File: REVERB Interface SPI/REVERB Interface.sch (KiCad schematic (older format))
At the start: 50 parts, among them J1 RPiZeroW, J2 Iridium, J3 APRS, J4 Antenna, M1 MountingHole_Pad, M2 MountingHole_Pad, M3 MountingHole_Pad, M4 MountingHole_Pad, M5 PiMount, M6 PiMount, M7 PiMount, M8 PiMount, U1 LSM9DS1BOB, U2 MAX3232, U3 SC16IS752IPW, Y1 1.8432MHz

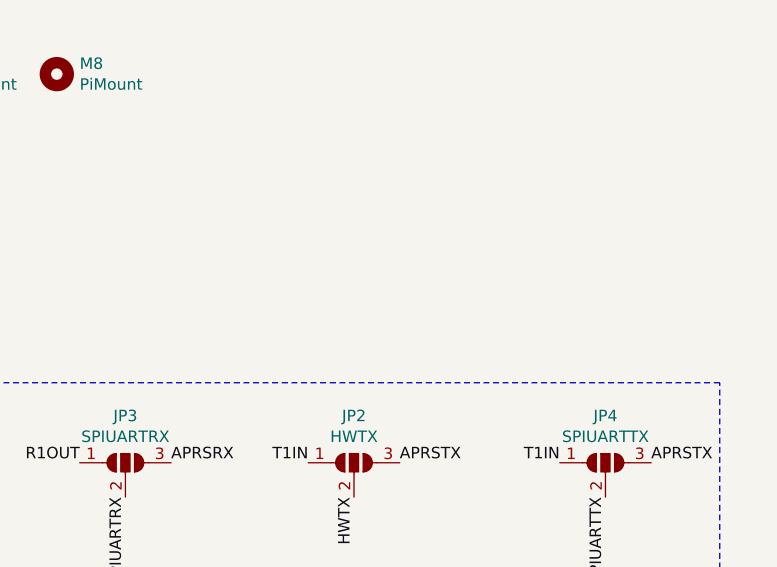
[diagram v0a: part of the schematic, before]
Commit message: Add LEDs for all used PDMs
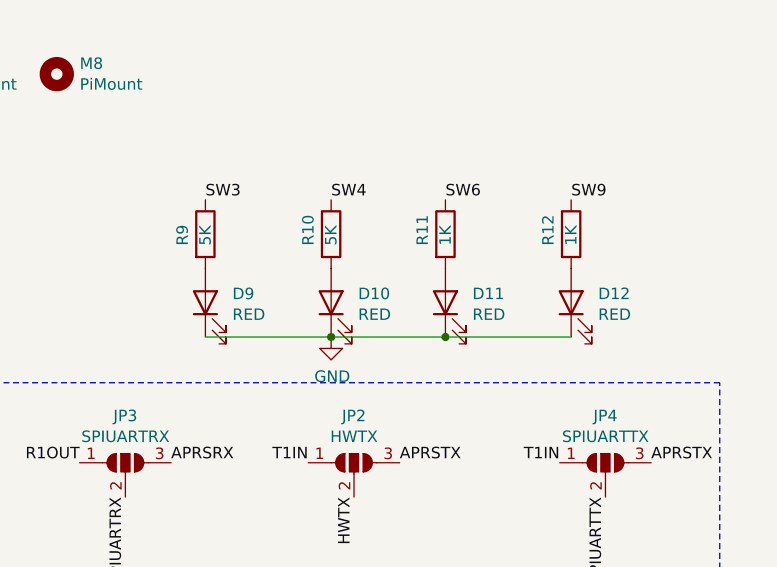
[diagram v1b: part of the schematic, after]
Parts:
- added D10, D11, D12, D9: RED, LED_SMD:LED_0805_2012Metric_Pad1.15x1.40mm_HandSolder, symbol Device:LED
- added R10, R9: 5K, Resistor_SMD:R_0805_2012Metric_Pad1.20x1.40mm_HandSolder, symbol Device:R
- added R11, R12: 1K, Resistor_SMD:R_0805_2012Metric_Pad1.20x1.40mm_HandSolder, symbol Device:R
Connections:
- net GND: now also D10.1 (K), D11.1 (K), D12.1 (K), D9.1 (K)
- net SW3: now also R9.1
- net SW4: now also R10.1
- net SW6: now also R11.1
- net SW9: now also R12.1
- new net: D9.2 (A), R9.2
- new net: D10.2 (A), R10.2
- new net: D11.2 (A), R11.2
- new net: D12.2 (A), R12.2
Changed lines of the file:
@@
 Text Label 6100 2150 0    50   ~ 0
 RTS
+$Comp
+L Device:LED D9
+U 1 1 6164D690
+P 9150 3200
+F 0 "D9" V 9189 3082 50  0000 R CNN
+F 1 "RED" V 9098 3082 50  0000 R CNN
+F 2 "LED_SMD:LED_0805_2012Metric_Pad1.15x1.40mm_HandSolder" H 9150 3200 50  0001 C CNN
+F 3 "~" H 9150 3200 50  0001 C CNN
+	1    9150 3200
+	0    -1   -1   0
+$EndComp
+$Comp
+L Device:R R9
+U 1 1 6164D696
+P 9150 2900
+F 0 "R9" V 9050 2850 50  0000 L CNN
+F 1 "5K" V 9150 2850 50  0000 L CNN
+F 2 "Resistor_SMD:R_0805_2012Metric_Pad1.20x1.40mm_HandSolder" V 9080 2900 50  0001 C CNN
+F 3 "~" H 9150 2900 50  0001 C CNN
+	1    9150 2900
+	1    0    0    -1
+$EndComp
+$Comp
+L Device:LED D10
+U 1 1 61656747
+P 9700 3200
+F 0 "D10" V 9739 3082 50  0000 R CNN
+F 1 "RED" V 9648 3082 50  0000 R CNN
+F 2 "LED_SMD:LED_0805_2012Metric_Pad1.15x1.40mm_HandSolder" H 9700 3200 50  0001 C CNN
+F 3 "~" H 9700 3200 50  0001 C CNN
+	1    9700 3200
+	0    -1   -1   0
+$EndComp
+$Comp
+L Device:R R10
+U 1 1 6165674D
+P 9700 2900
+F 0 "R10" V 9600 2850 50  0000 L CNN
+F 1 "5K" V 9700 2850 50  0000 L CNN
+F 2 "Resistor_SMD:R_0805_2012Metric_Pad1.20x1.40mm_HandSolder" V 9630 2900 50  0001 C CNN
+F 3 "~" H 9700 2900 50  0001 C CNN
+	1    9700 2900
+	1    0    0    -1
+$EndComp
+$Comp
+L Device:LED D11
+U 1 1 6165A88F
+P 10200 3200
+F 0 "D11" V 10239 3082 50  0000 R CNN
+F 1 "RED" V 10148 3082 50  0000 R CNN
+F 2 "LED_SMD:LED_0805_2012Metric_Pad1.15x1.40mm_HandSolder" H 10200 3200 50  0001 C CNN
+F 3 "~" H 10200 3200 50  0001 C CNN
+	1    10200 3200
+	0    -1   -1   0
+$EndComp
+$Comp
+L Device:R R11
+U 1 1 6165A895
+P 10200 2900
+F 0 "R11" V 10100 2850 50  0000 L CNN
+F 1 "1K" V 10200 2850 50  0000 L CNN
+F 2 "Resistor_SMD:R_0805_2012Metric_Pad1.20x1.40mm_HandSolder" V 10130 2900 50  0001 C CNN
+F 3 "~" H 10200 2900 50  0001 C CNN
+	1    10200 2900
+	1    0    0    -1
+$EndComp
+Text Label 9150 2750 0    50   ~ 0
+SW3
+Text Label 9700 2750 0    50   ~ 0
+SW4
+Text Label 10200 2750 0    50   ~ 0
+SW6
+Wire Wire Line
+	9150 3350 9700 3350
+Connection ~ 9700 3350
+Wire Wire Line
+	9700 3350 10200 3350
+$Comp
+L power:GND #PWR?
+U 1 1 61664C9F
+P 9700 3350
+F 0 "#PWR?" H 9700 3100 50  0001 C CNN
+F 1 "GND" H 9705 3177 50  0000 C CNN
+F 2 "" H 9700 3350 50  0001 C CNN
+F 3 "" H 9700 3350 50  0001 C CNN
+	1    9700 3350
+	1    0    0    -1
+$EndComp
+$Comp
+L Device:LED D12
+U 1 1 61666765
+P 10750 3200
+F 0 "D12" V 10789 3082 50  0000 R CNN
+F 1 "RED" V 10698 3082 50  0000 R CNN
+F 2 "LED_SMD:LED_0805_2012Metric_Pad1.15x1.40mm_HandSolder" H 10750 3200 50  0001 C CNN
+F 3 "~" H 10750 3200 50  0001 C CNN
+	1    10750 3200
+	0    -1   -1   0
+$EndComp
+$Comp
+L Device:R R12
+U 1 1 6166676B
+P 10750 2900
+F 0 "R12" V 10650 2850 50  0000 L CNN
+F 1 "1K" V 10750 2850 50  0000 L CNN
+F 2 "Resistor_SMD:R_0805_2012Metric_Pad1.20x1.40mm_HandSolder" V 10680 2900 50  0001 C CNN
+F 3 "~" H 10750 2900 50  0001 C CNN
+	1    10750 2900
+	1    0    0    -1
+$EndComp
+Text Label 10750 2750 0    50   ~ 0
+SW9
+Wire Wire Line
+	10200 3350 10750 3350
+Connection ~ 10200 3350
 $EndSCHEMATC

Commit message: Replace max3232 footprint, update stencil
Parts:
- U2: footprint REVERB Interface:Texas_Instruments-MAX3232ID -> REVERB Interface:Texas_Instruments-MAX3232ID-Level_A
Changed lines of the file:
@@
 F 0 "U2" H 5850 6731 50  0000 C CNN
 F 1 "MAX3232" H 5850 6640 50  0000 C CNN
-F 2 "REVERB Interface:Texas_Instruments-MAX3232ID" H 5900 4300 50  0001 L CNN
+F 2 "REVERB Interface:Texas_Instruments-MAX3232ID-Level_A" H 5900 4300 50  0001 L CNN
 F 3 "https://datasheets.maximintegrated.com/en/ds/MAX3222-MAX3241.pdf" H 5850 5450 50  0001 C CNN
 	1    5850 5350
@@
 	9700 3350 10200 3350
 $Comp
-L power:GND #PWR?
+L power:GND #PWR0135
 U 1 1 61664C9F
 P 9700 3350
-F 0 "#PWR?" H 9700 3100 50  0001 C CNN
+F 0 "#PWR0135" H 9700 3100 50  0001 C CNN
 F 1 "GND" H 9705 3177 50  0000 C CNN
 F 2 "" H 9700 3350 50  0001 C CNN

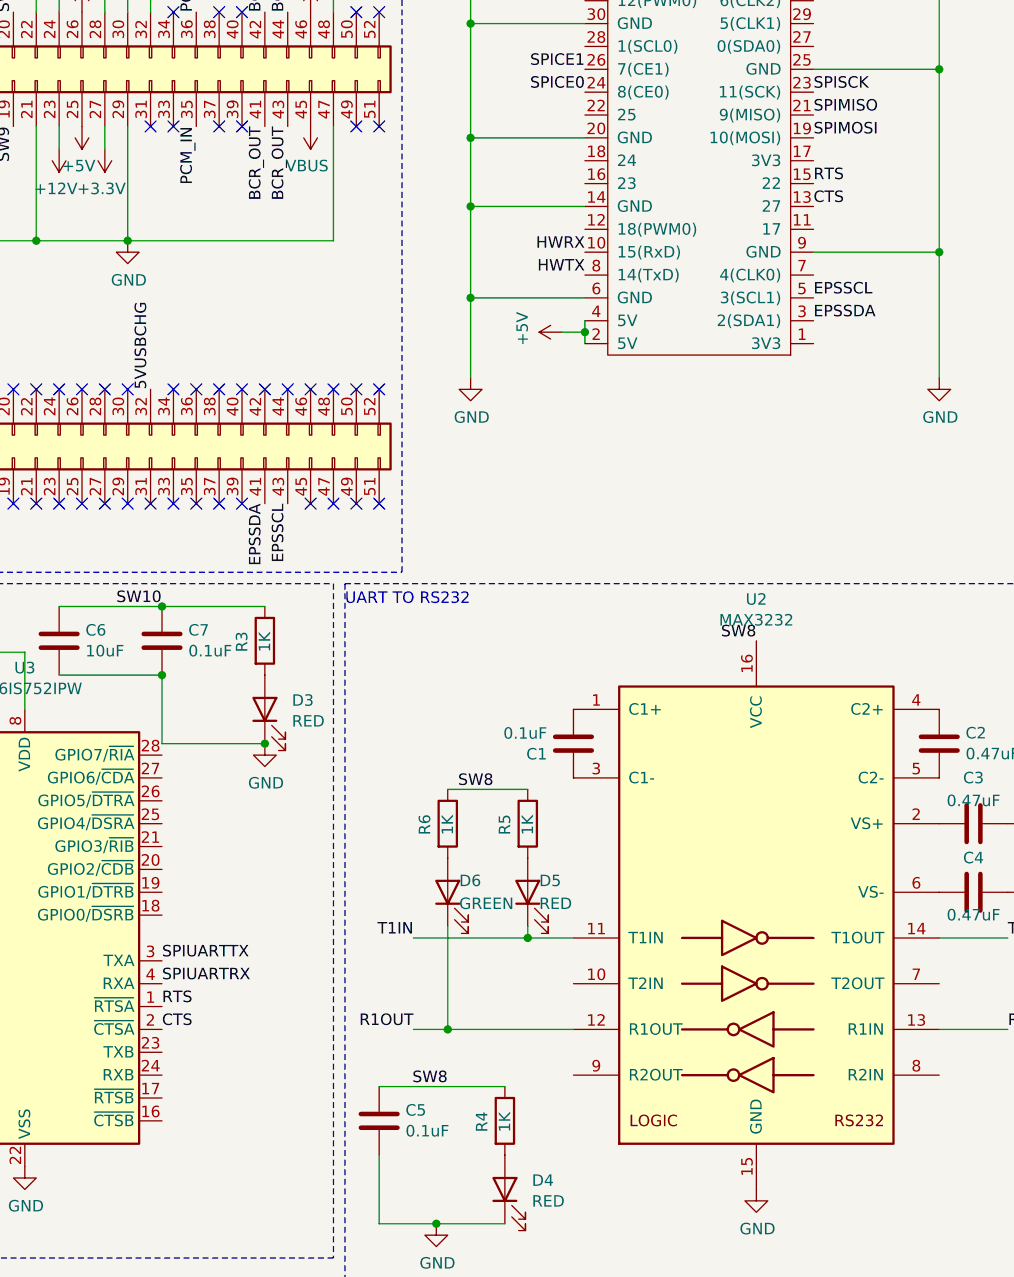
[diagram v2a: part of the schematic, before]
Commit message: Remove incorrect uart flow control connections, pull CTS low. Improve silkscreen placement
Issue #3 and Issue #5
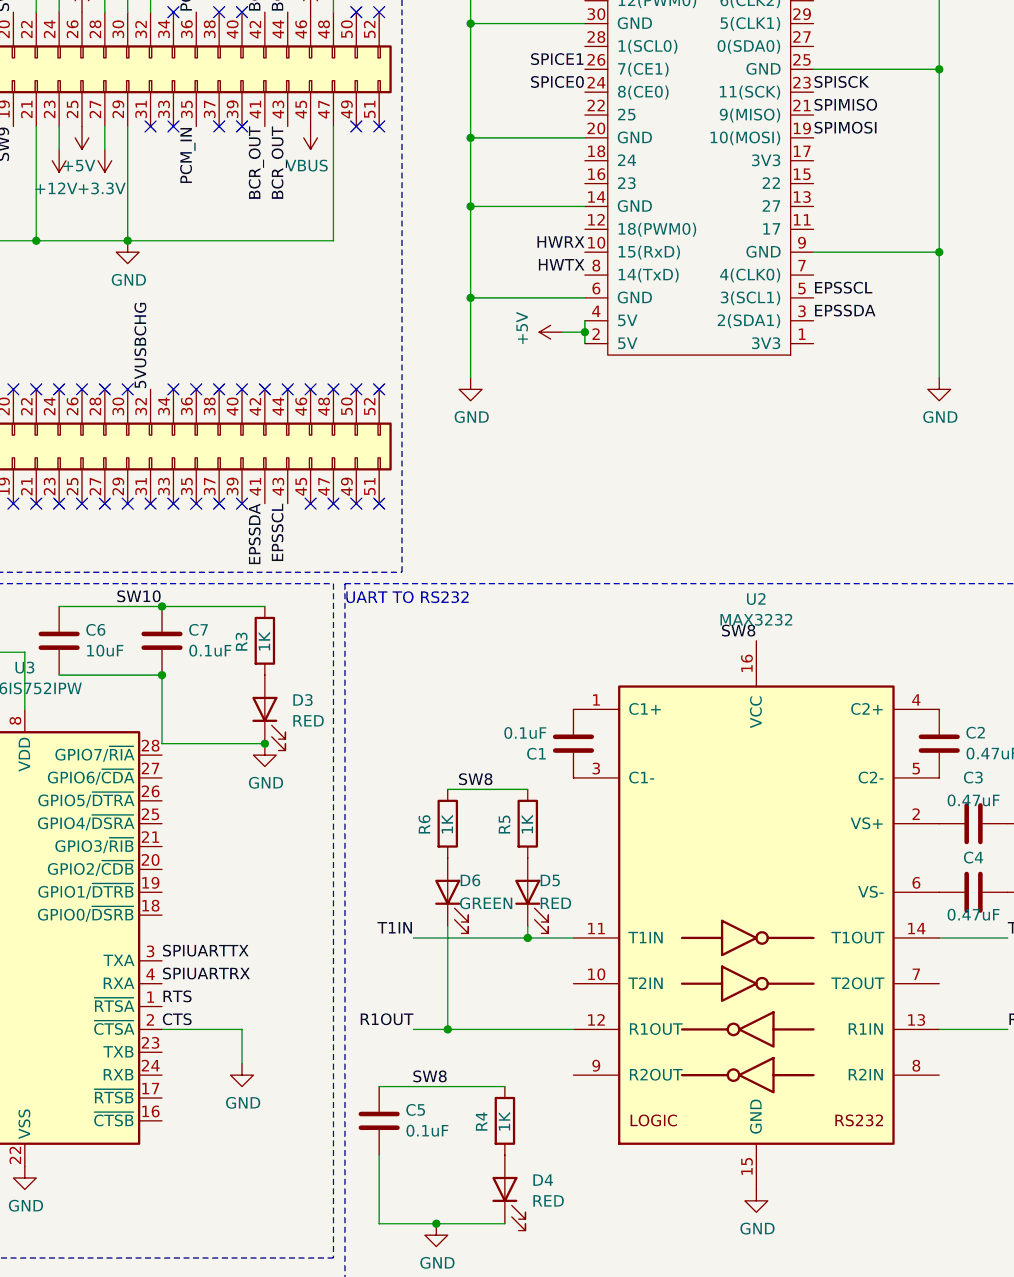
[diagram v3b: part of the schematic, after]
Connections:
- net GND: now also U3.2 (~CTSA)
- net RTS: no longer J1.15 (22)
- net CTS: no longer names the net of J1.13 (27)
- net CTS: no longer U3.2 (~CTSA)
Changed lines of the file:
@@
 Wire Notes Line
 	4000 6850 850  6850
-Text Label 3250 5850 0    50   ~ 0
-CTS
-Text Label 3250 5750 0    50   ~ 0
-RTS
-Text Label 6100 2250 0    50   ~ 0
-CTS
-Text Label 6100 2150 0    50   ~ 0
-RTS
 $Comp
 L Device:LED D9
@@
 	10200 3350 10750 3350
 Connection ~ 10200 3350
+Text Label 3250 5750 0    50   ~ 0
+RTS
+Text Label 3250 5850 0    50   ~ 0
+CTS
+Wire Wire Line
+	3250 5850 3600 5850
+Wire Wire Line
+	3600 5850 3600 6000
+$Comp
+L power:GND #PWR?
+U 1 1 61769C75
+P 3600 6000
+F 0 "#PWR?" H 3600 5750 50  0001 C CNN
+F 1 "GND" H 3605 5827 50  0000 C CNN
+F 2 "" H 3600 6000 50  0001 C CNN
+F 3 "" H 3600 6000 50  0001 C CNN
+	1    3600 6000
+	1    0    0    -1
+$EndComp
 $EndSCHEMATC

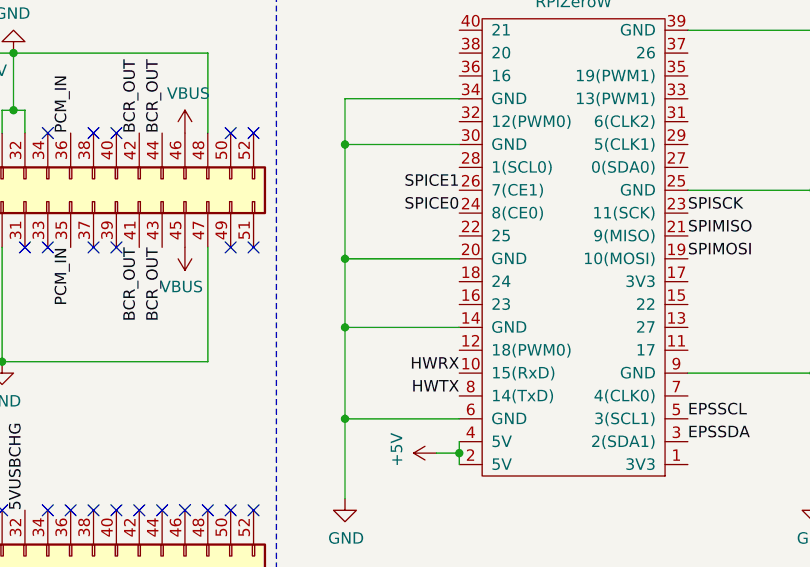
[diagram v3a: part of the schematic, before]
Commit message: Add bitbang uart connections
gpio 23 and 24, #2
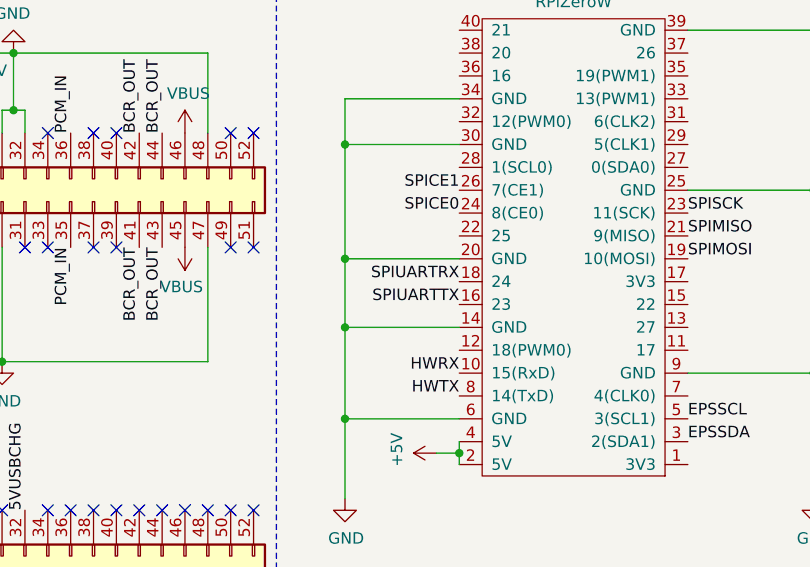
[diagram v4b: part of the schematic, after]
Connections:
- net SPIUARTRX: now also J1.18 (24)
- net SPIUARTTX: now also J1.16 (23)
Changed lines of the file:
@@
 	1    0    0    -1
 $EndComp
+Text Label 5100 2050 2    50   ~ 0
+SPIUARTRX
+Text Label 5100 2150 2    50   ~ 0
+SPIUARTTX
 $EndSCHEMATC

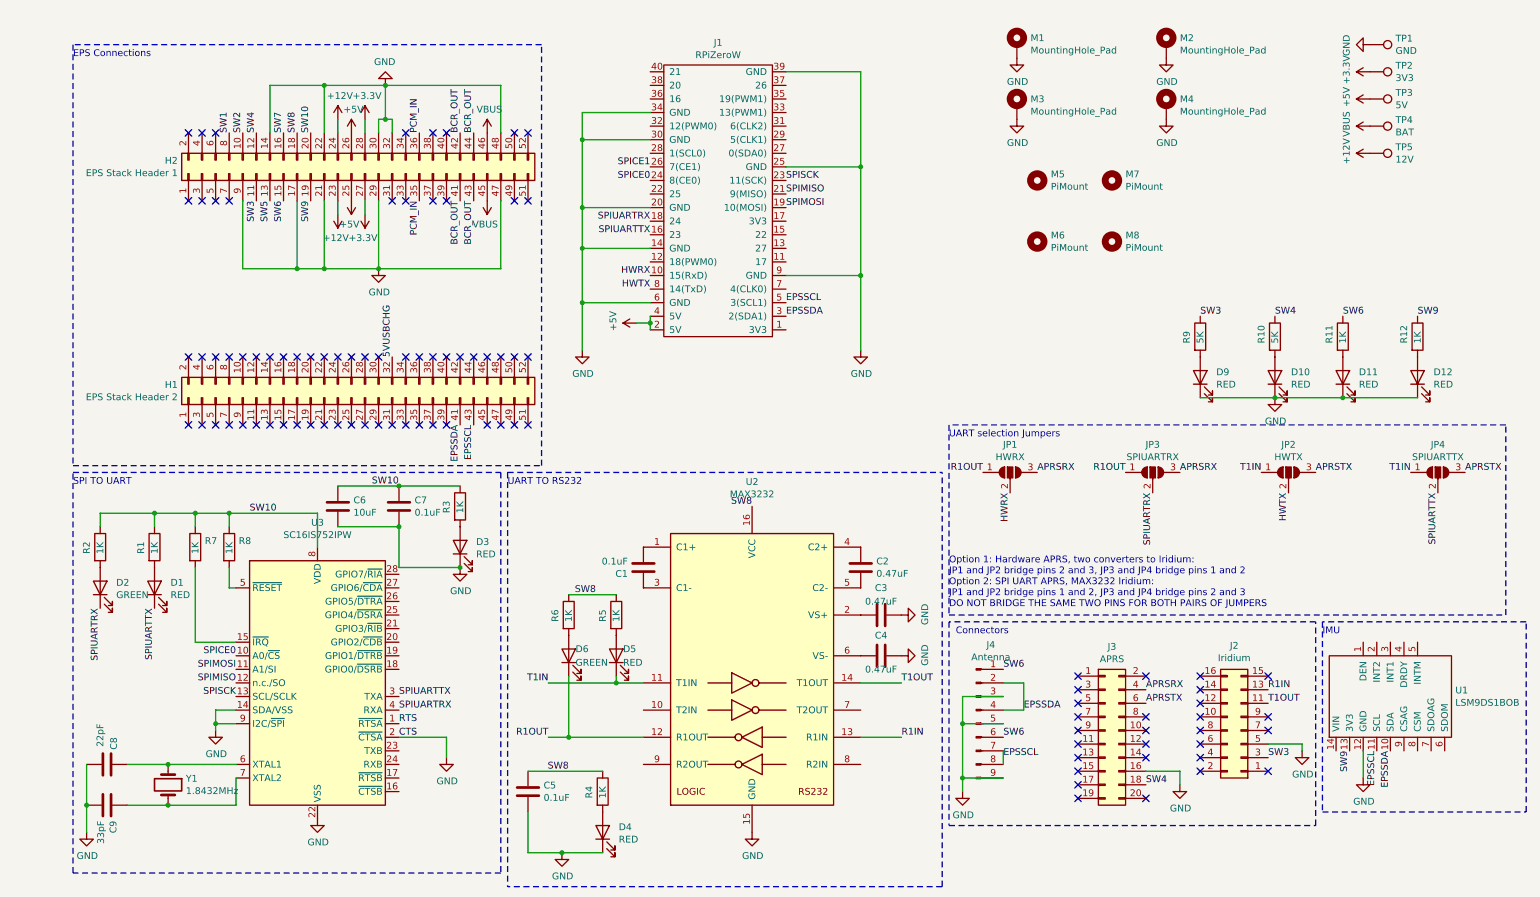
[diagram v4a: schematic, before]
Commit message: Add level shifters, updated sch revision numbers consistent with pcb
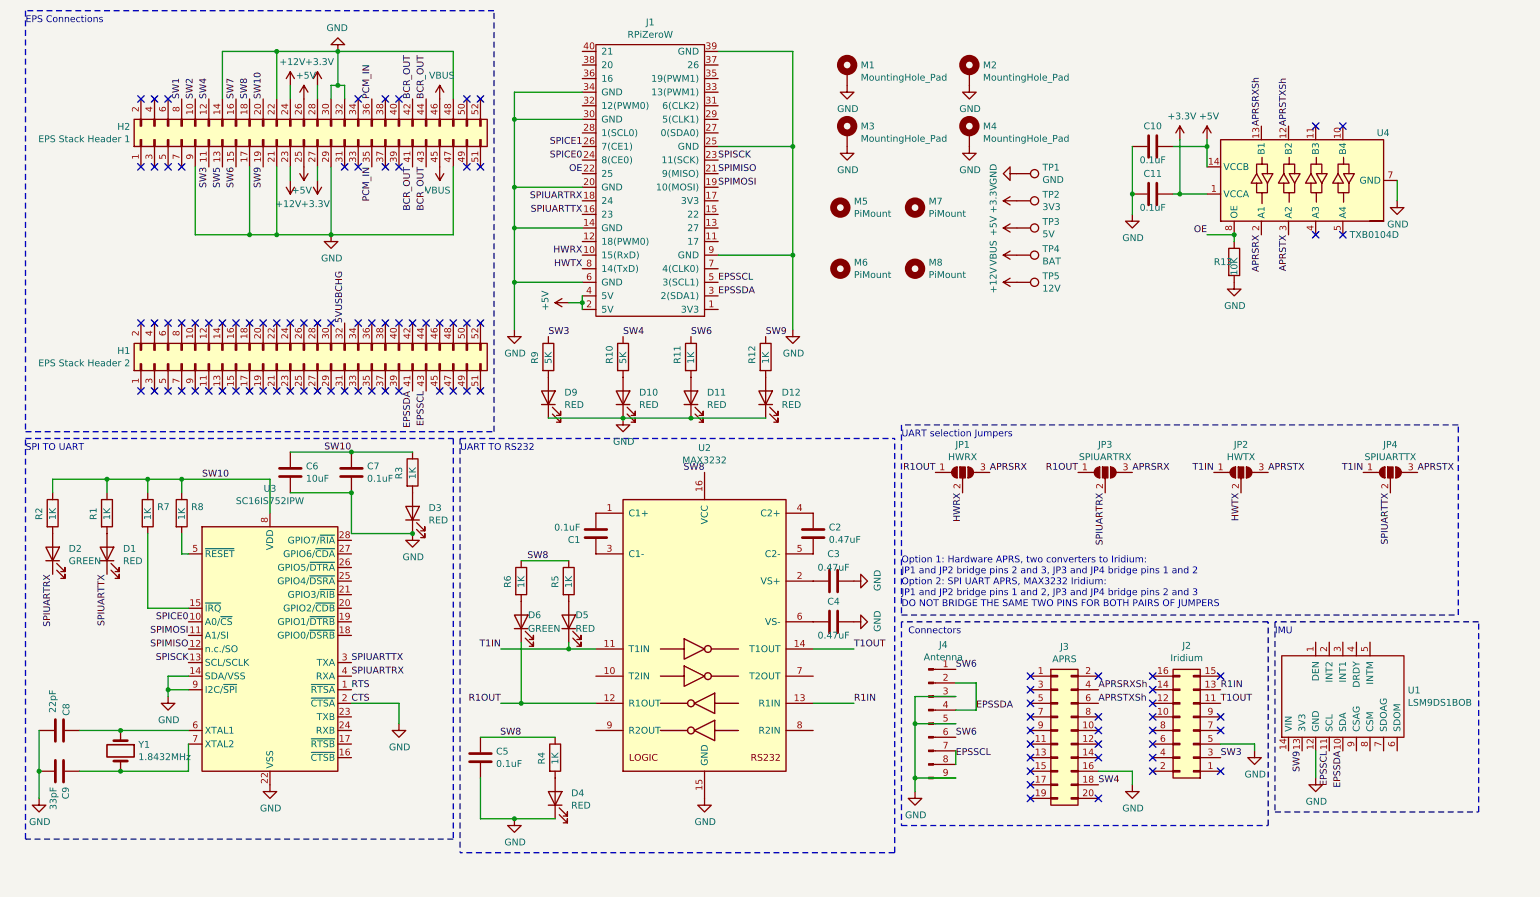
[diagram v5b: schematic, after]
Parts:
- added C10, C11: 0.1uF, symbol Device:C
- added R13: 10K, symbol Device:R
- added U4: TXB0104D, Package_SO:SOIC-14_3.9x8.7mm_P1.27mm, symbol Logic_LevelTranslator:TXB0104D
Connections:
- net +3V3: now also C11.1, U4.1 (VCCA)
- net +5V: now also C10.1, U4.14 (VCCB)
- net APRSRX: now also U4.2 (A1); no longer J3.4 (Pin_4)
- net APRSTX: now also U4.3 (A2); no longer J3.6 (Pin_6)
- net GND: now also C10.2, C11.2, R13.2, U4.7 (GND)
- net OE: now reaches J1.22 (25)
- net OE: now also R13.1, U4.8 (OE)
- new net APRSRXSh: J3.4 (Pin_4), U4.13 (B1)
- new net APRSTXSh: J3.6 (Pin_6), U4.12 (B2)
- no-connect marks 95 -> 99
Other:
- moved on the sheet: C1, C2, C3, C4, C5, C6, C7, C8, C9, D1, D10, D11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

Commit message: add level shifter to routing
#1
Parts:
- C10, C11: footprint (none) -> Capacitor_SMD:C_0805_2012Metric_Pad1.18x1.45mm_HandSolder
- R13: footprint (none) -> Resistor_SMD:R_0805_2012Metric_Pad1.20x1.40mm_HandSolder
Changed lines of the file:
@@
 F 0 "C10" V 8650 1500 50  0000 C CNN
 F 1 "0.1uF" V 8900 1500 50  0000 C CNN
-F 2 "" H 8838 1350 50  0001 C CNN
+F 2 "Capacitor_SMD:C_0805_2012Metric_Pad1.18x1.45mm_HandSolder" H 8838 1350 50  0001 C CNN
 F 3 "~" H 8800 1500 50  0001 C CNN
 	1    8800 1500
@@
 F 0 "C11" V 8650 1850 50  0000 C CNN
 F 1 "0.1uF" V 8900 1850 50  0000 C CNN
-F 2 "" H 8838 1700 50  0001 C CNN
+F 2 "Capacitor_SMD:C_0805_2012Metric_Pad1.18x1.45mm_HandSolder" H 8838 1700 50  0001 C CNN
 F 3 "~" H 8800 1850 50  0001 C CNN
 	1    8800 1850
@@
 F 0 "R13" H 9250 2350 50  0000 L CNN
 F 1 "10K" V 9400 2250 50  0000 L CNN
-F 2 "" V 9330 2350 50  0001 C CNN
+F 2 "Resistor_SMD:R_0805_2012Metric_Pad1.20x1.40mm_HandSolder" V 9330 2350 50  0001 C CNN
 F 3 "~" H 9400 2350 50  0001 C CNN
 	1    9400 2350
